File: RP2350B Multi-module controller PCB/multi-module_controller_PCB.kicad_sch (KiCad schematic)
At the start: 87 parts, among them J1 Conn_02x06_Odd_Even, J10 Internal unused GPIO Breakout, J2 Conn_02x26_Odd_Even, J3 Conn_02x26_Odd_Even, J4 SM03B-SRSS-TB, J5 USB_C_Receptacle_USB2.0_14P, J6 USB_C_Receptacle_USB2.0_14P, J7 Module_Bay, J8 USB_A, J9 ADC_Breakout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

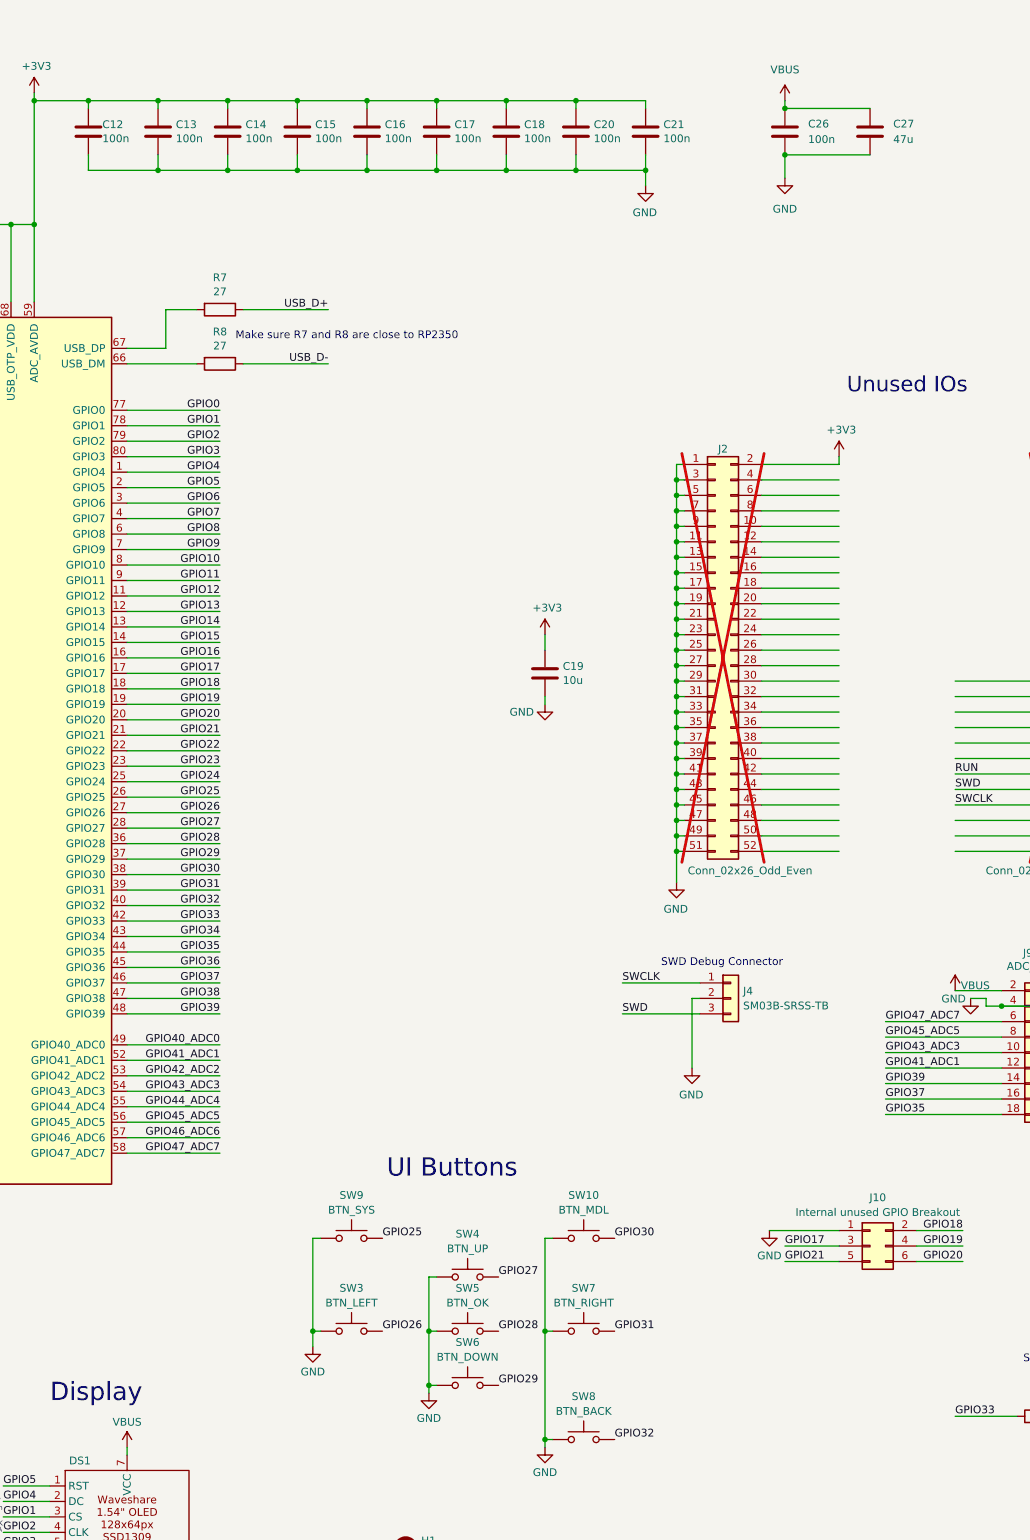
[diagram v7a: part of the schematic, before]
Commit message: update PCB to drive OLED from 3v3 rail
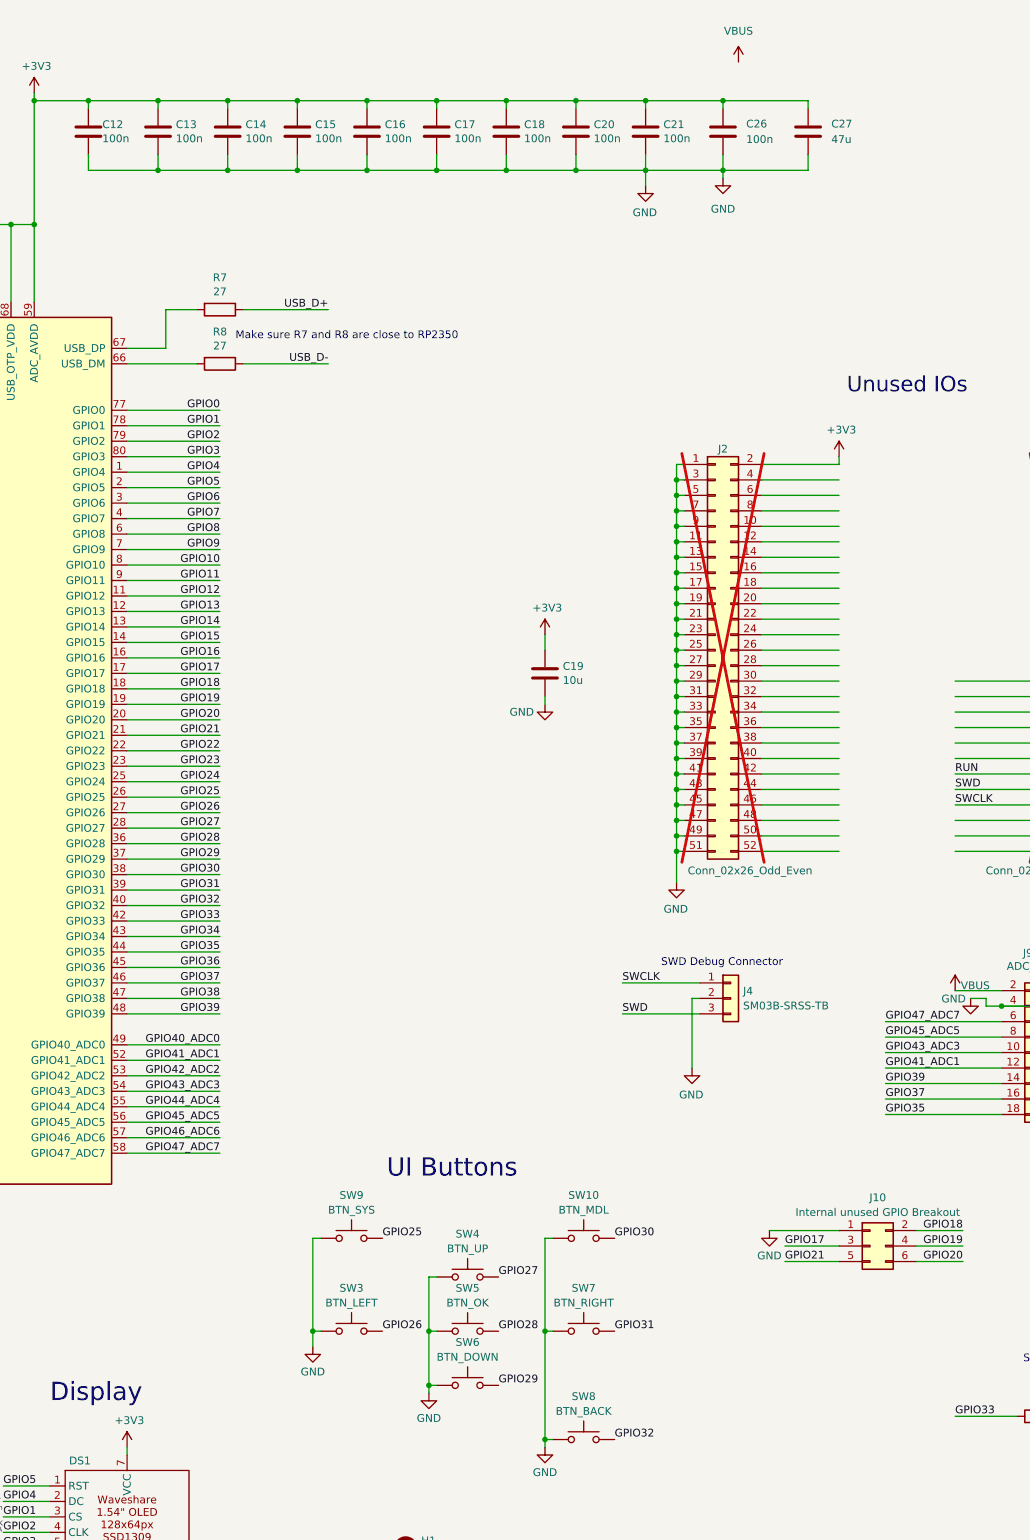
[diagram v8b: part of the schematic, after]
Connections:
- net +3V3: now also C26.1, C27.1, DS1.7 (VCC)
- net VBUS: no longer C26.1, C27.1, DS1.7 (VCC)
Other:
- moved on the sheet: C26, C27
